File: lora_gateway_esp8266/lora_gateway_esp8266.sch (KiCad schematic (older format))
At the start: 10 parts, among them J1 Conn_01x03_Male, J2 Conn_Coaxial, SW1 SW_Push, SW2 SW_Push, U1 ESP-12E, U2 RFM95W-868S2

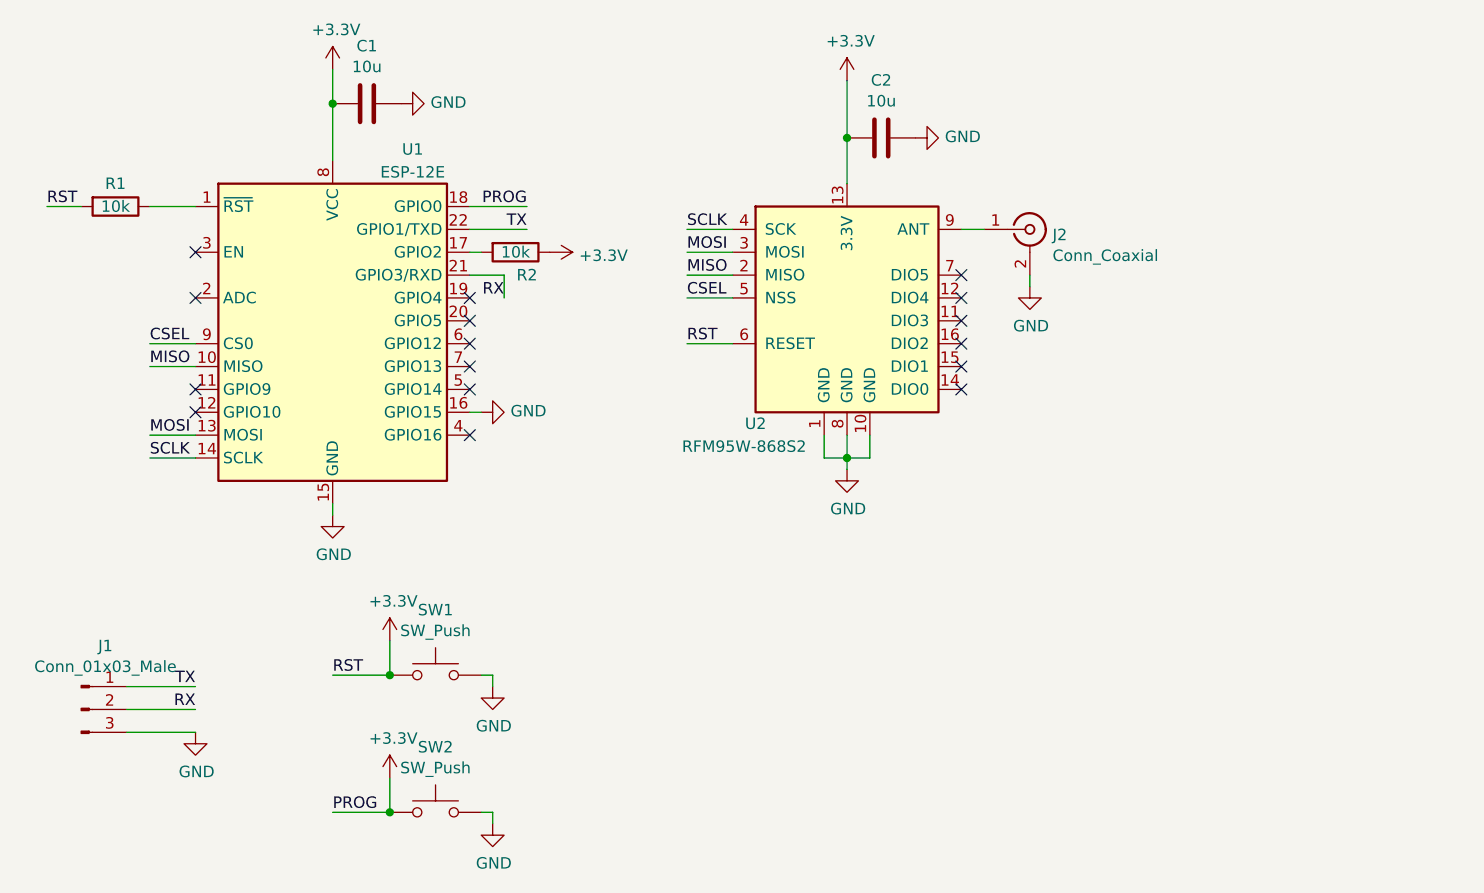
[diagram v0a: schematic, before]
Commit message: edited error in schematic, created netlist
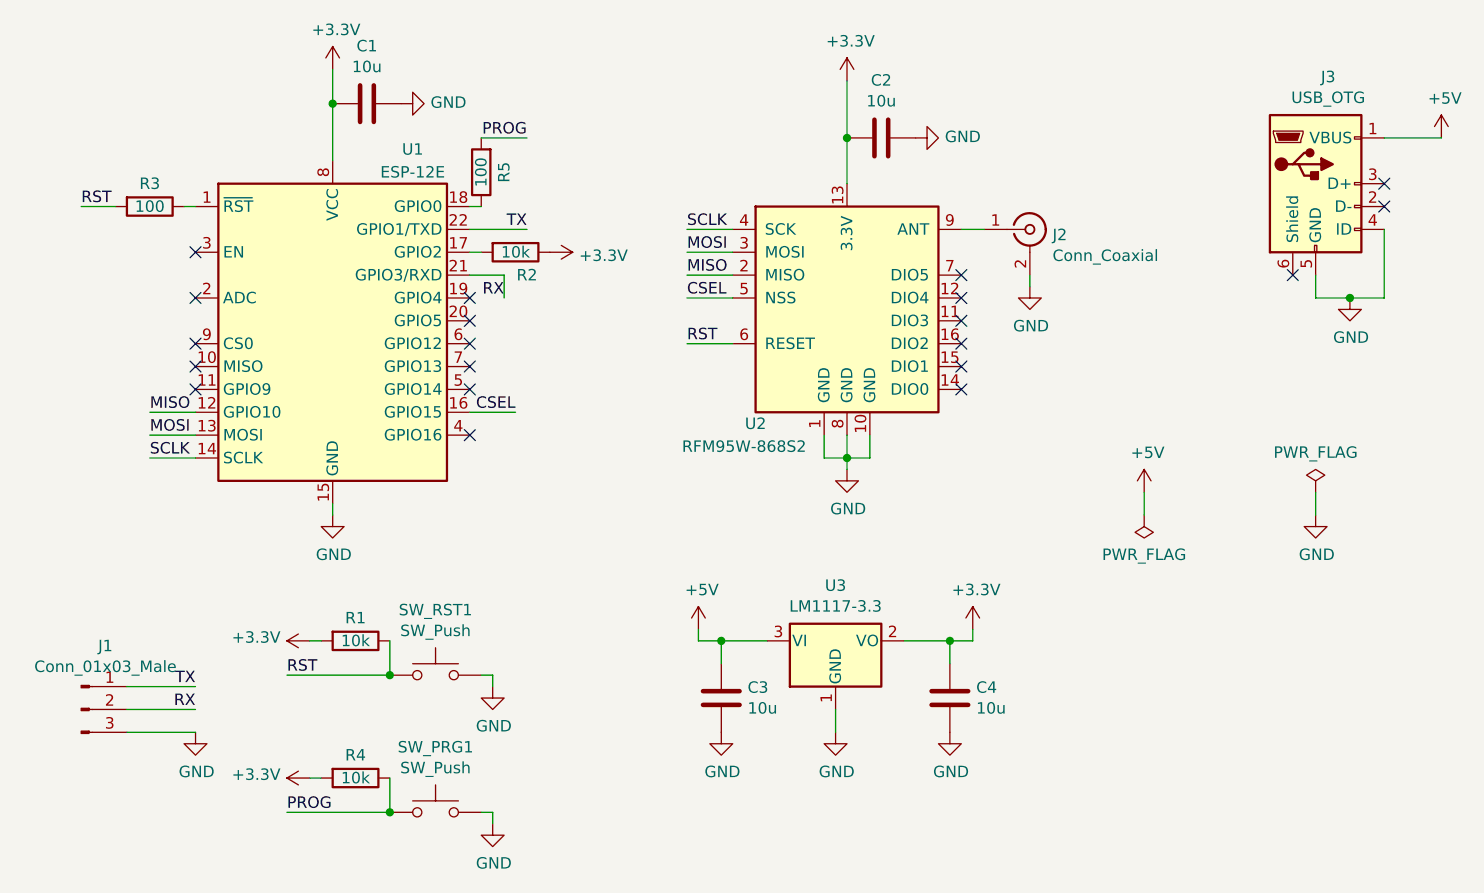
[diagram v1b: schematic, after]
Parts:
- added C3, C4: 10u, Capacitor_SMD:C_1206_3216Metric_Pad1.42x1.75mm_HandSolder, symbol Device:C
- added J3: USB_OTG, Connector_USB:USB_Mini-B_Lumberg_2486_01_Horizontal, symbol Connector:USB_OTG
- added R3, R5: 100, Resistor_SMD:R_1206_3216Metric_Pad1.42x1.75mm_HandSolder, symbol Device:R
- added R4: 10k, Resistor_SMD:R_1206_3216Metric_Pad1.42x1.75mm_HandSolder, symbol Device:R
- added U3: LM1117-3.3, Package_TO_SOT_SMD:SOT-223, symbol Regulator_Linear:LM1117-3.3
- J1: footprint (none) -> Connector_PinHeader_1.00mm:PinHeader_1x03_P1.00mm_Horizontal
- SW_PRG1: renamed from SW2; footprint (none) -> Button_Switch_THT:SW_PUSH_6mm
- SW_RST1: renamed from SW1; footprint (none) -> Button_Switch_THT:SW_PUSH_6mm
- U2: footprint (none) -> RF_Module:HOPERF_RFM9XW_SMD
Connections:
- net +3V3: now also C4.1, R4.2, U3.2 (VO); no longer SW_PRG1.1, SW_RST1.1, U1.18 (GPIO0), U2.6 (RESET)
- net CSEL: now also U1.16 (GPIO15); no longer U1.9 (CS0)
- net GND: now also C3.2, C4.2, J3.4 (ID), J3.5 (GND), U3.1 (GND); no longer U1.16 (GPIO15)
- net MISO: now also U1.12 (GPIO10); no longer U1.10 (MISO)
- net at U1.1 (~RST): now also R3.1; no longer R1.1
- new net: R5.1, U1.18 (GPIO0)
- new net +5V: C3.1, J3.1 (VBUS), U3.3 (VI)
- new net PROG: R4.1, R5.2, SW_PRG1.1
- new net RST: R1.1, R3.2, SW_RST1.1, U2.6 (RESET)
- no-connect marks 16 -> 20
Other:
- moved on the sheet: R1
